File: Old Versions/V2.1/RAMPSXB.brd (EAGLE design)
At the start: 129.5 x 73.5 mm, 97 parts, among them CN1 1X4-BIG, CN2 1X4-BIG, CN3 1X4-BIG, CN4 1X4-BIG, CN5 1X4-BIG, CN6 1X4-BIG, CN7 1X4-BIG, CN8 1X4-BIG, CN9 1X4-BIG, J1 1X2-3.5MM, J2 1X2-3.5MM, J3 1X2-3.5MM, J4 1X2-3.5MM, J5 1X2-3.5MM, Q1 PSMN7R0-30YLC, Q2 PSMN7R0-30YLC, Q3 PSMN7R0-30YLC, Q4 PSMN7R0-30YLC

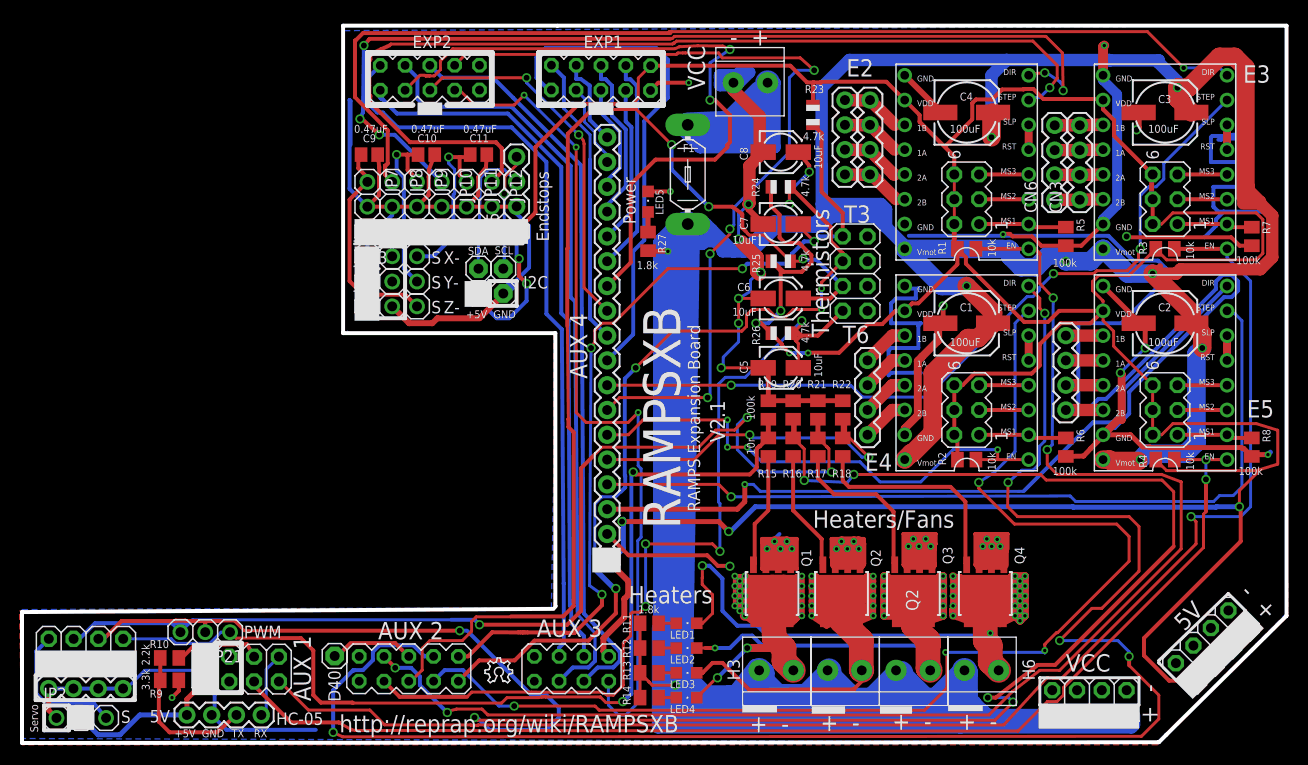
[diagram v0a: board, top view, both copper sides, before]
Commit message: Replaced FETs with PSMN7R0-30YLCs for production.
Added Older Version Directory for the old STP55 board. It should also
work as well.
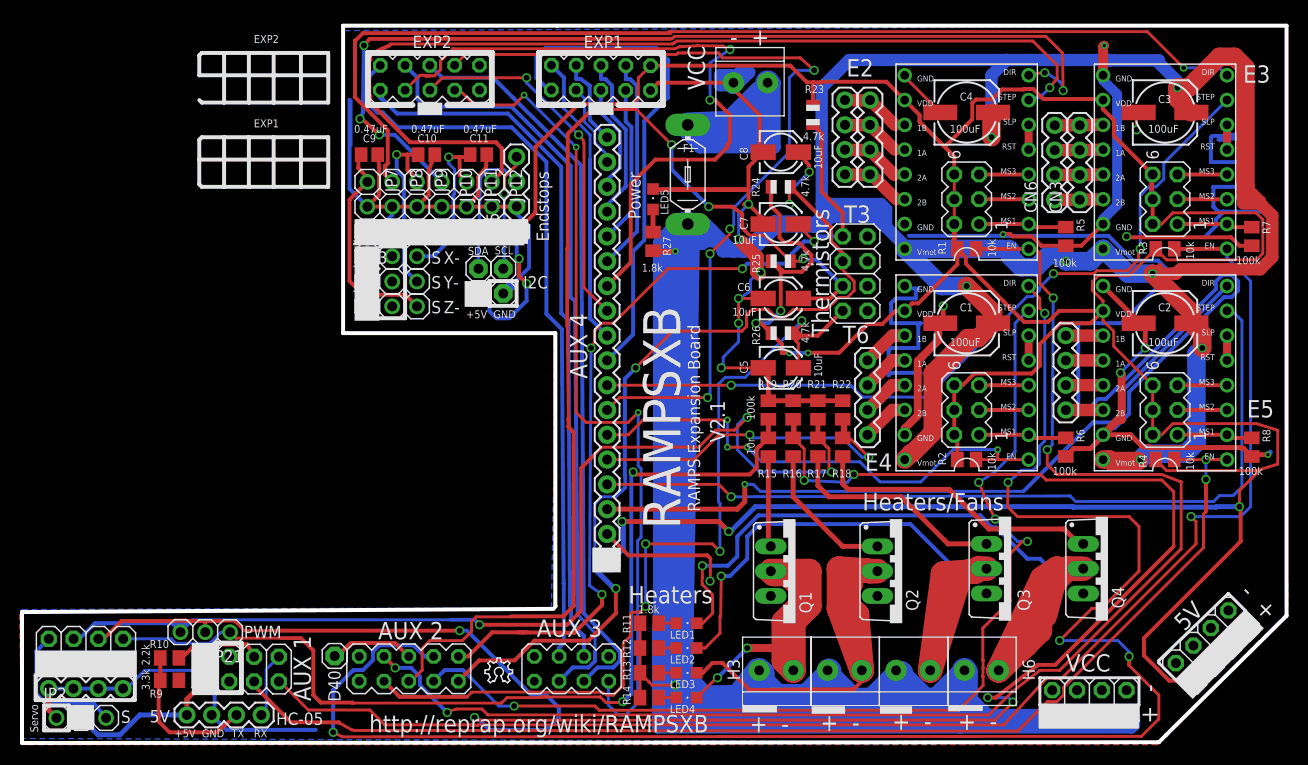
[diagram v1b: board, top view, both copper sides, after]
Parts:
- Q1, Q2, Q3, Q4: value PSMN7R0-30YLC -> IRF512; device MyLibrary:LFPAK -> transistor-power:TO220BV
- moved Q4 12.8 mm to (79.1, 17.0), turned to 270 degrees
- moved Q3 10.3 mm to (69.2, 17.0), turned to 270 degrees
- moved Q2 6.63 mm to (58.0, 16.8), turned to 270 degrees
- moved Q1 3.32 mm to (47.1, 16.8), turned to 270 degrees
- moved LED5 0.57 mm to (32.5, 54.9)
- moved R27 0.51 mm to (32.5, 50.5)
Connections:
- removed net N$45: Q3.4, R17.1
- new net GND1: R10.1
- new net N$49: Q1.G, R15.1
- net GND: now also Q1.S, Q2.S, Q3.S, Q4.S; no longer Q1.1, Q1.2, Q1.3, Q2.1, Q2.2, Q2.3, Q3.1, Q3.2, Q3.3, Q4.1, Q4.2, Q4.3, R10.1
- net N$30: now also Q1.D; no longer Q1.5
- net N$36: now also Q2.D; no longer Q2.5
- net N$37: now also Q3.D; no longer Q3.5
- net N$38: now also Q4.D; no longer Q4.5
- net N$46: now also Q2.G, R16.1; no longer Q4.4, R18.1
- net N$47: now also Q3.G, R17.1; no longer Q2.4, R16.1
- net N$48: now also Q4.G, R18.1; no longer Q1.4, R15.1
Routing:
- net GND: track 631.8 -> 478.6 mm, vias 38 -> 15
- net N$36: track 108.6 -> 44.3 mm, vias 10 -> 0
- net N$30: track 97.2 -> 39.2 mm, vias 20 -> 2
- net N$38: track 105.3 -> 84.3 mm, vias 22 -> 1
- net D44: track 123.2 -> 104.8 mm
- net N$48: track 11.7 -> 29.9 mm
- net N$45: track 16.9 -> 0.00 mm
- net +5V: track 483.0 -> 471.3 mm
- net N$47: track 12.4 -> 22.7 mm
- net N$49: track 0.00 -> 9.32 mm
- net N$46: track 22.5 -> 14.9 mm
- net N$37: track 68.4 -> 65.7 mm, vias 11 -> 1
- net A12: track 99.0 -> 101.2 mm, vias 6 -> 4
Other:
- board text added: "Q1"
- board text added: "Q3"
- board text added: "Q4"

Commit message: Fixed LED Numbering, updated V2.1
LED Indicators were not on the right FETs. Not sure how I missed that.
Updated V2.1 with corrected Vector Text.
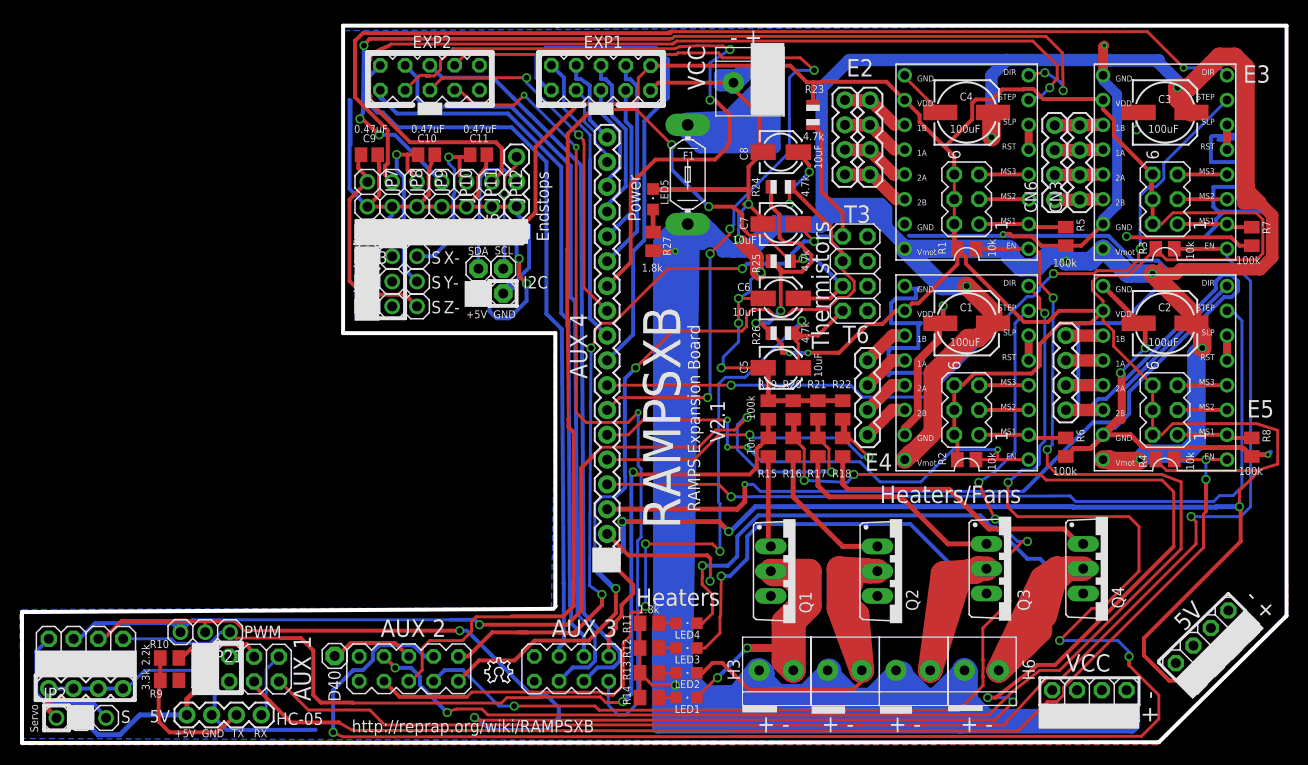
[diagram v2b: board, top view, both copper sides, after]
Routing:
- net +5V: track 471.3 -> 483.4 mm
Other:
- board text added: "(C) Scott Ziv"

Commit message: Fixed some issues with V2.1, and updated gerbers
fixed some stuff with V2.1 and corrected some issues
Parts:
- added LOGO2: OSHW-LOGOL, SparkFun-Aesthetics:OSHW-LOGO-L
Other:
- board text added: "D42"
- board text added: "Developed by S.Z."
- board text removed: "(C) Scott Ziv"
